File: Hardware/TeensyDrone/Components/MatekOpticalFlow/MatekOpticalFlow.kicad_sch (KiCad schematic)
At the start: 4 parts, among them J1 Conn_02x02_Odd_Even, U1 STM32L051C8Tx

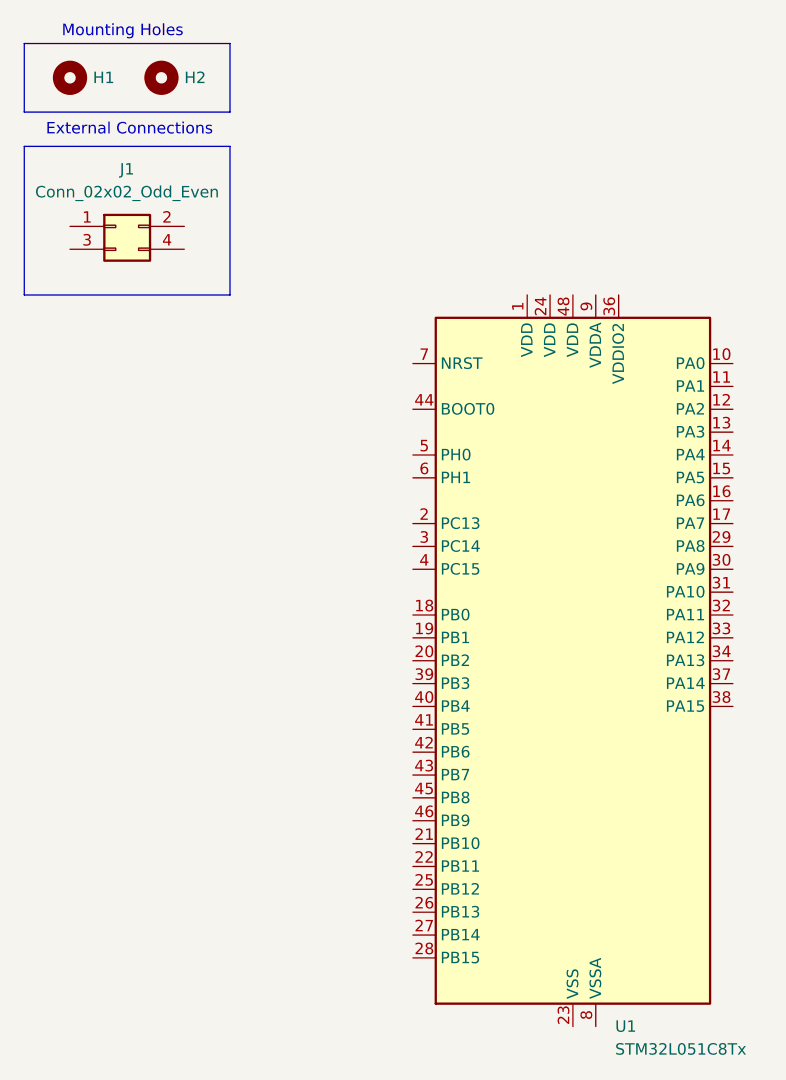
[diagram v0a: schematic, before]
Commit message: Moved to Teensy 4.0 from 4.1
Signed-off-by: lucas <mtglucas1@gmail.com>
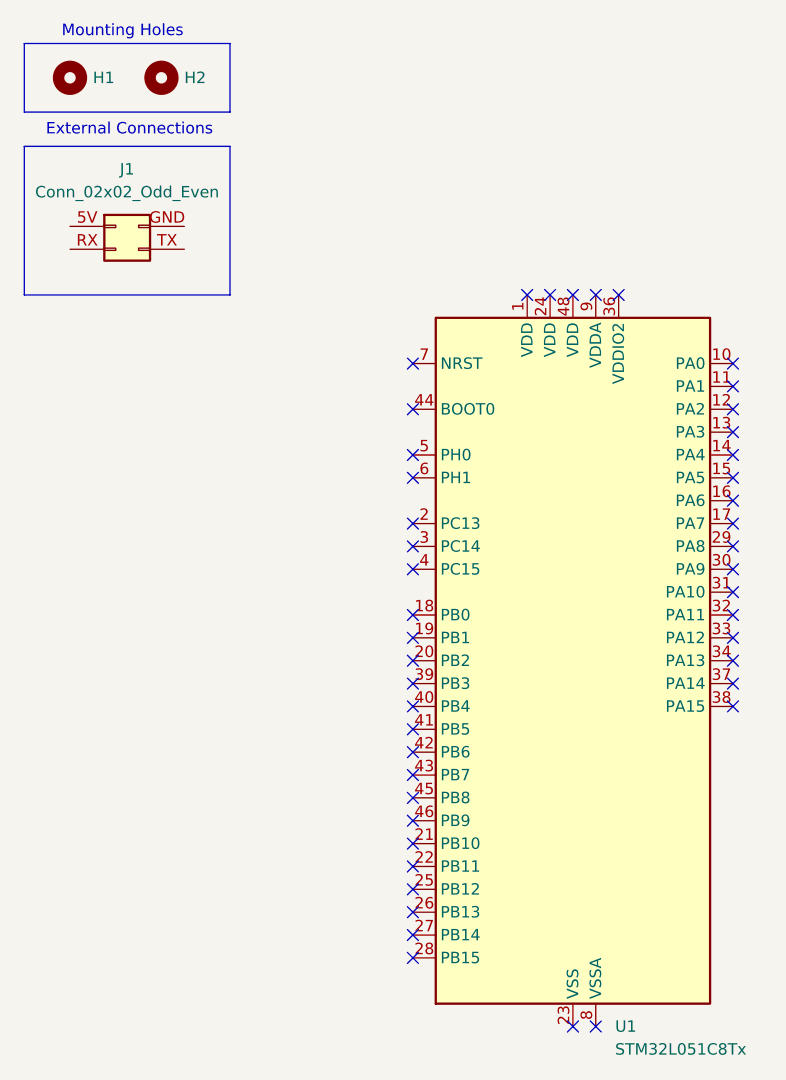
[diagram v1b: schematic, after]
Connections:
- no-connect marks 0 -> 46
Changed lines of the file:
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@@
 		)
+	)
+	(no_connect
+		(at 59.69 114.3)
+	)
+	(no_connect
+		(at 95.25 86.36)
+	)
+	(no_connect
+		(at 59.69 86.36)
+	)
+	(no_connect
+		(at 59.69 106.68)
+	)
+	(no_connect
+		(at 72.39 43.18)
+	)
+	(no_connect
+		(at 95.25 73.66)
+	)
+	(no_connect
+		(at 95.25 53.34)
+	)
+	(no_connect
+		(at 59.69 50.8)
+	)
+	(no_connect
+		(at 95.25 60.96)
+	)
+	(no_connect
+		(at 95.25 76.2)
+	)
+	(no_connect
+		(at 95.25 83.82)
+	)
+	(no_connect
+		(at 59.69 99.06)
+	)
+	(no_connect
+		(at 59.69 73.66)
+	)
+	(no_connect
+		(at 95.25 58.42)
+	)
+	(no_connect
+		(at 59.69 63.5)
+	)
+	(no_connect
+		(at 59.69 91.44)
+	)
+	(no_connect
+		(at 59.69 96.52)
+	)
+	(no_connect
+		(at 59.69 111.76)
+	)
+	(no_connect
+		(at 95.25 66.04)
+	)
+	(no_connect
+		(at 59.69 55.88)
+	)
+	(no_connect
+		(at 59.69 93.98)
+	)
+	(no_connect
+		(at 77.47 43.18)
+	)
+	(no_connect
+		(at 59.69 116.84)
+	)
+	(no_connect
+		(at 59.69 68.58)
+	)
+	(no_connect
+		(at 95.25 55.88)
+	)
+	(no_connect
+		(at 74.93 43.18)
+	)
+	(no_connect
+		(at 95.25 78.74)
+	)
+	(no_connect
+		(at 95.25 63.5)
+	)
+	(no_connect
+		(at 82.55 43.18)
+	)
+	(no_connect
+		(at 59.69 104.14)
+	)
+	(no_connect
+		(at 95.25 81.28)
+	)
+	(no_connect
+		(at 95.25 50.8)
+	)
+	(no_connect
+		(at 80.01 43.18)
+	)
+	(no_connect
+		(at 80.01 124.46)
+	)
+	(no_connect
+		(at 59.69 109.22)
+	)
+	(no_connect
+		(at 59.69 101.6)
+	)
+	(no_connect
+		(at 95.25 71.12)
+	)
+	(no_connect
+		(at 59.69 88.9)
+	)
+	(no_connect
+		(at 77.47 124.46)
+	)
+	(no_connect
+		(at 59.69 71.12)
+	)
+	(no_connect
+		(at 95.25 88.9)
+	)
+	(no_connect
+		(at 59.69 78.74)
+	)
+	(no_connect
+		(at 59.69 83.82)
+	)
+	(no_connect
+		(at 59.69 60.96)
+	)
+	(no_connect
+		(at 95.25 68.58)
+	)
+	(no_connect
+		(at 59.69 81.28)
 	)
 	(symbol
@@
 			)
 		)
-		(pin "4"
-		)
-		(pin "2"
-		)
-		(pin "1"
-		)
-		(pin "3"
+		(pin "5V"
+		)
+		(pin "TX"
+		)
+		(pin "RX"
+		)
+		(pin "GND"
 		)
 		(instances

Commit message: Revert "Moved to Teensy 4.0 from 4.1"
This reverts commit 64f42becbd12878e856e1dc259d1d069ff850610.
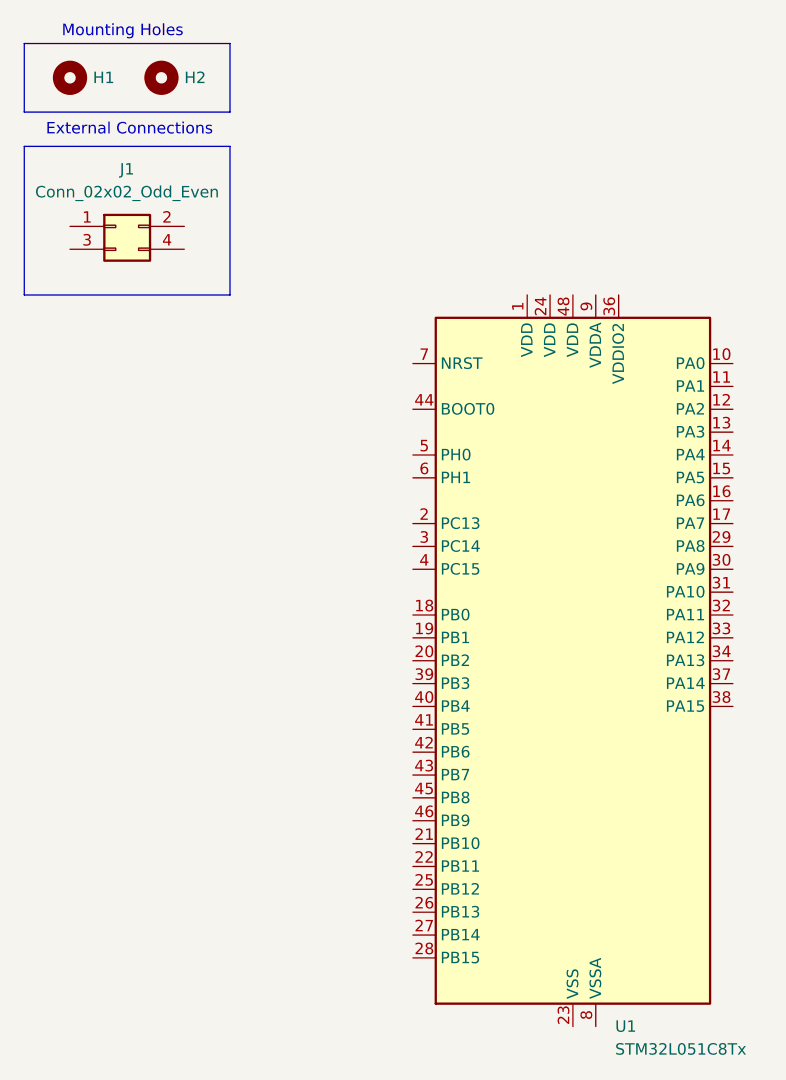
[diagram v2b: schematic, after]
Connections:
- no-connect marks 46 -> 0
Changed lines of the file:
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@@
 		)
-	)
-	(no_connect
-		(at 59.69 114.3)
-	)
-	(no_connect
-		(at 95.25 86.36)
-	)
-	(no_connect
-		(at 59.69 86.36)
-	)
-	(no_connect
-		(at 59.69 106.68)
-	)
-	(no_connect
-		(at 72.39 43.18)
-	)
-	(no_connect
-		(at 95.25 73.66)
-	)
-	(no_connect
-		(at 95.25 53.34)
-	)
-	(no_connect
-		(at 59.69 50.8)
-	)
-	(no_connect
-		(at 95.25 60.96)
-	)
-	(no_connect
-		(at 95.25 76.2)
-	)
-	(no_connect
-		(at 95.25 83.82)
-	)
-	(no_connect
-		(at 59.69 99.06)
-	)
-	(no_connect
-		(at 59.69 73.66)
-	)
-	(no_connect
-		(at 95.25 58.42)
-	)
-	(no_connect
-		(at 59.69 63.5)
-	)
-	(no_connect
-		(at 59.69 91.44)
-	)
-	(no_connect
-		(at 59.69 96.52)
-	)
-	(no_connect
-		(at 59.69 111.76)
-	)
-	(no_connect
-		(at 95.25 66.04)
-	)
-	(no_connect
-		(at 59.69 55.88)
-	)
-	(no_connect
-		(at 59.69 93.98)
-	)
-	(no_connect
-		(at 77.47 43.18)
-	)
-	(no_connect
-		(at 59.69 116.84)
-	)
-	(no_connect
-		(at 59.69 68.58)
-	)
-	(no_connect
-		(at 95.25 55.88)
-	)
-	(no_connect
-		(at 74.93 43.18)
-	)
-	(no_connect
-		(at 95.25 78.74)
-	)
-	(no_connect
-		(at 95.25 63.5)
-	)
-	(no_connect
-		(at 82.55 43.18)
-	)
-	(no_connect
-		(at 59.69 104.14)
-	)
-	(no_connect
-		(at 95.25 81.28)
-	)
-	(no_connect
-		(at 95.25 50.8)
-	)
-	(no_connect
-		(at 80.01 43.18)
-	)
-	(no_connect
-		(at 80.01 124.46)
-	)
-	(no_connect
-		(at 59.69 109.22)
-	)
-	(no_connect
-		(at 59.69 101.6)
-	)
-	(no_connect
-		(at 95.25 71.12)
-	)
-	(no_connect
-		(at 59.69 88.9)
-	)
-	(no_connect
-		(at 77.47 124.46)
-	)
-	(no_connect
-		(at 59.69 71.12)
-	)
-	(no_connect
-		(at 95.25 88.9)
-	)
-	(no_connect
-		(at 59.69 78.74)
-	)
-	(no_connect
-		(at 59.69 83.82)
-	)
-	(no_connect
-		(at 59.69 60.96)
-	)
-	(no_connect
-		(at 95.25 68.58)
-	)
-	(no_connect
-		(at 59.69 81.28)
 	)
 	(symbol
@@
 			)
 		)
-		(pin "5V"
-		)
-		(pin "TX"
-		)
-		(pin "RX"
-		)
-		(pin "GND"
+		(pin "4"
+		)
+		(pin "2"
+		)
+		(pin "1"
+		)
+		(pin "3"
 		)
 		(instances
